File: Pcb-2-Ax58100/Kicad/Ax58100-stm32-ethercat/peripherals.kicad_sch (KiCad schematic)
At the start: 18 parts, among them J10 DAC1, J11 Encoder 1, J12 Encoder 2, J13 Encoder 3, J14 Encoder 4, J9 I2C bus2

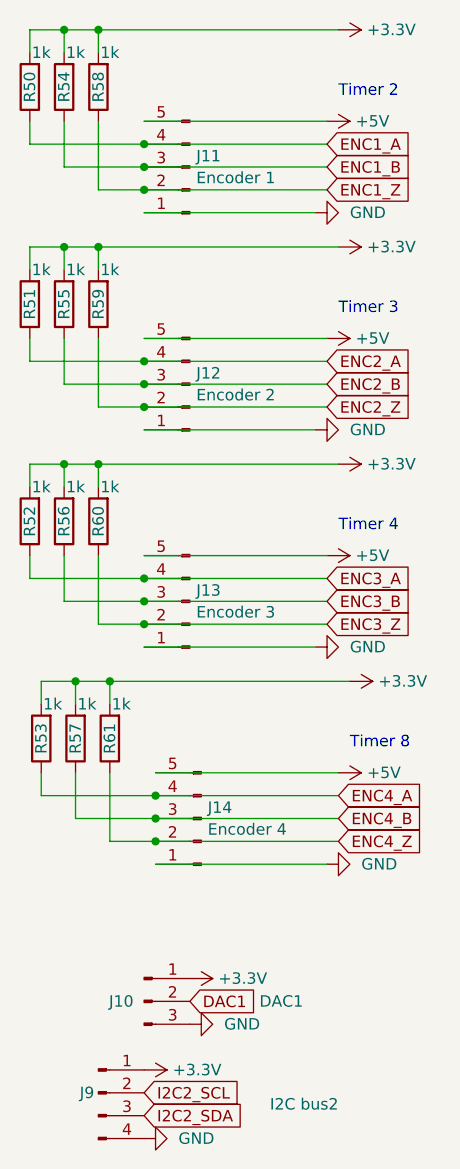
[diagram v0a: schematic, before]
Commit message: Geographic annotation on pcb 2
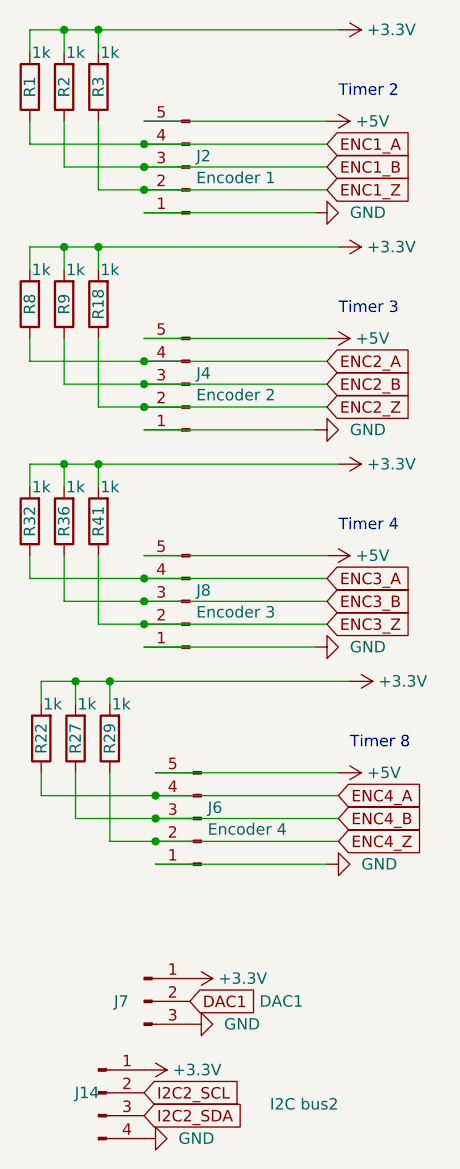
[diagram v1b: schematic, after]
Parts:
- renumbered J9 to J14, J11 to J2, J12 to J4, J14 to J6, J10 to J7, J13 to J8, R50 to R1, R59 to R18, R54 to R2, R53 to R22, R57 to R27, R61 to R29, R58 to R3, R52 to R32, R56 to R36, R60 to R41, R51 to R8, R55 to R9
